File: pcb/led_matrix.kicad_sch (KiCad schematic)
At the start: 8 parts

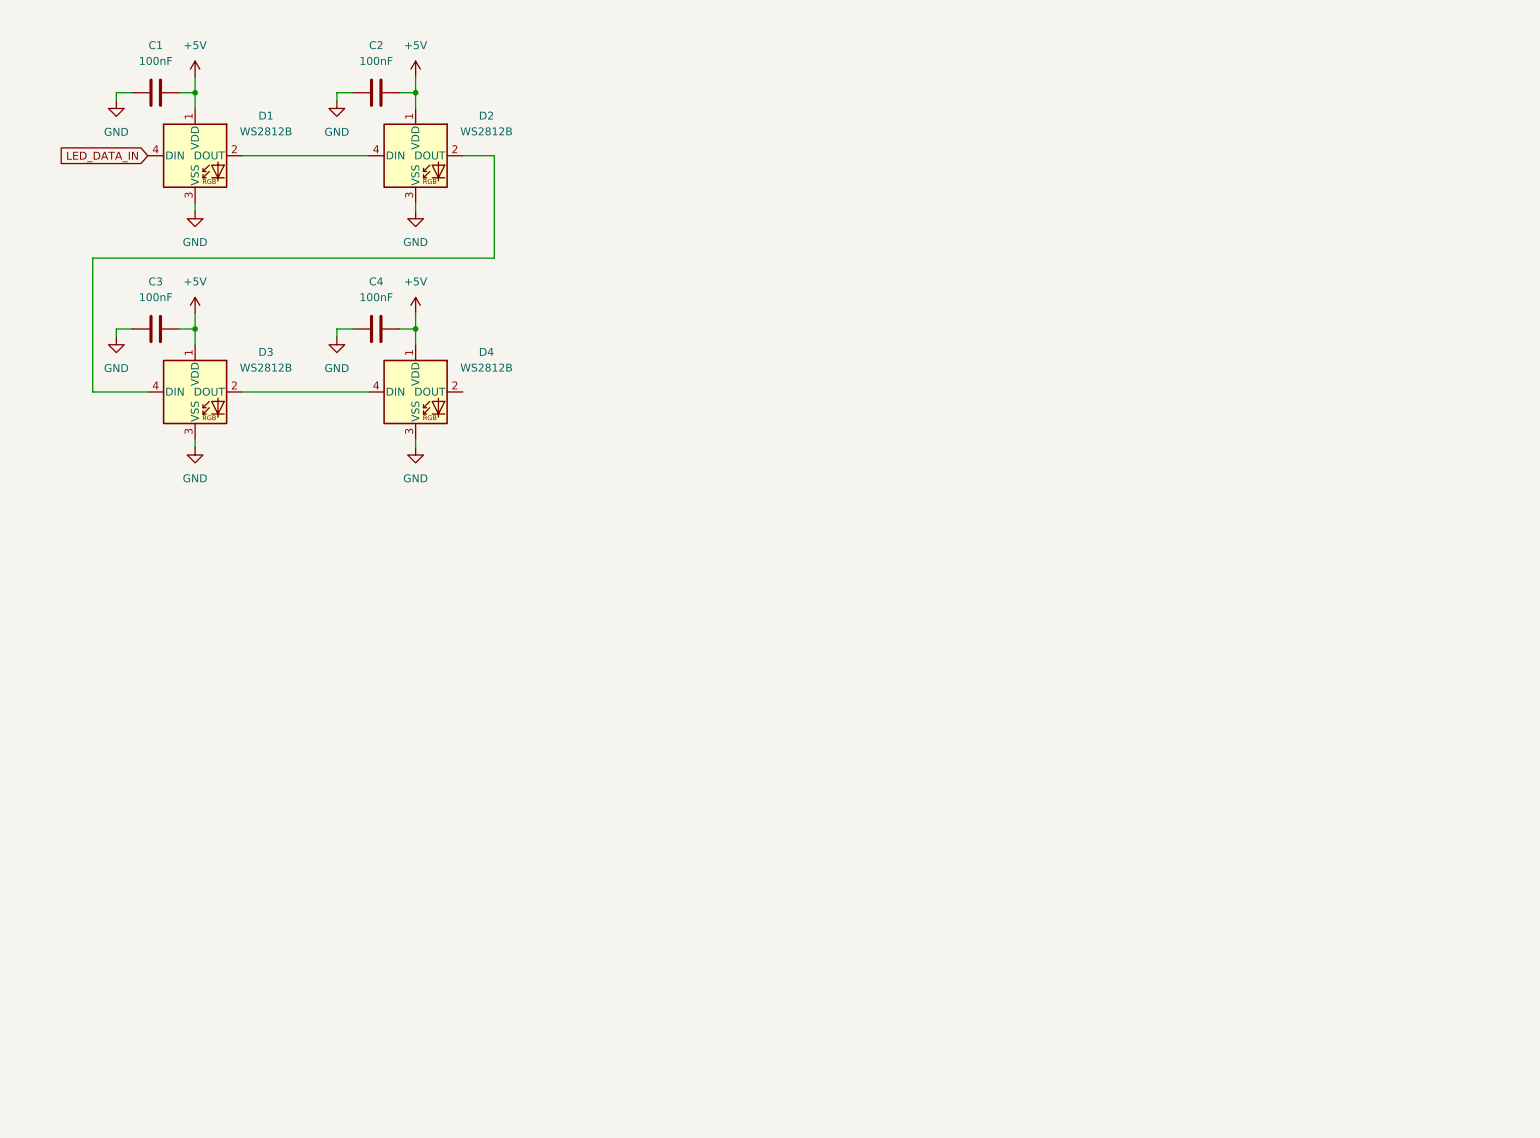
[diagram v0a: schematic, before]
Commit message: connect all components in schematic, only 13 LEDs for now
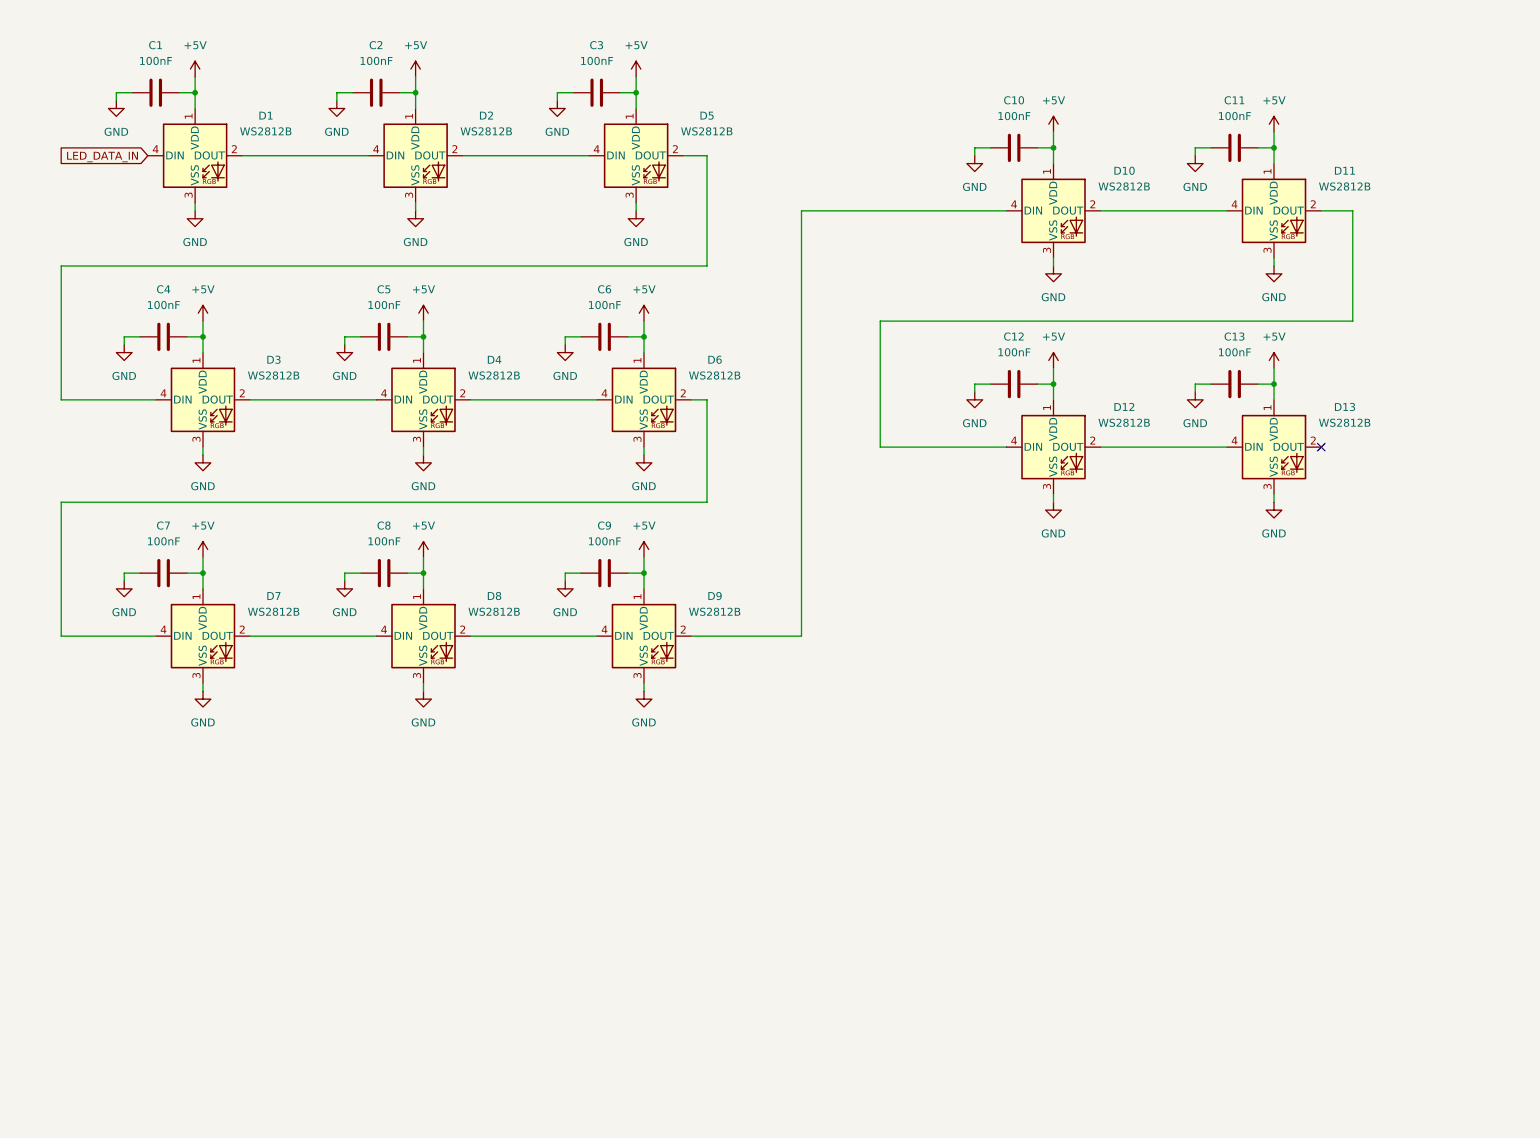
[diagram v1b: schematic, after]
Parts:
- added C10, C11, C12, C13, C5, C6, C7, C8, C9: 100nF, symbol Device:C
- added D10, D11, D12, D13, D5, D6, D7, D8, D9: WS2812B, LED_SMD:LED_WS2812B_PLCC4_5.0x5.0mm_P3.2mm, symbol LED:WS2812B
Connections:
- net +5V: now also C10.2, C11.2, C12.2, C13.2, C5.2, C6.2, C7.2, C8.2, C9.2, D10.1 (VDD), D11.1 (VDD), D12.1 (VDD), D13.1 (VDD), D5.1 (VDD), D6.1 (VDD), D7.1 (VDD), D8.1 (VDD), D9.1 (VDD)
- net GND: now also C10.1, C11.1, C12.1, C13.1, C5.1, C6.1, C7.1, C8.1, C9.1, D10.3 (VSS), D11.3 (VSS), D12.3 (VSS), D13.3 (VSS), D5.3 (VSS), D6.3 (VSS), D7.3 (VSS), D8.3 (VSS), D9.3 (VSS)
- net at D4.2 (DOUT): now also D6.4 (DIN)
- net at D2.2 (DOUT): now also D5.4 (DIN); no longer D3.4 (DIN)
- new net: D3.4 (DIN), D5.2 (DOUT)
- new net: D8.2 (DOUT), D9.4 (DIN)
- new net: D7.2 (DOUT), D8.4 (DIN)
- new net: D10.2 (DOUT), D11.4 (DIN)
- new net: D10.4 (DIN), D9.2 (DOUT)
- new net: D12.2 (DOUT), D13.4 (DIN)
- new net: D6.2 (DOUT), D7.4 (DIN)
- new net: D11.2 (DOUT), D12.4 (DIN)
- no-connect marks 0 -> 1

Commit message: add description to schematic sheets
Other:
- title: (none) -> Project Mora Jai
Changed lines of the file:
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@@
 	(generator_version "9.0")
 	(paper "A4")
+	(title_block
+		(title "Project Mora Jai")
+		(date "2026-02-04")
+		(rev "1")
+		(comment 1 "CERN-OHL-S-2.0")
+	)
 	(junction
 		(at 45.72 66.04)

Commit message: start PCB dimensions
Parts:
- C1, C10, C11, C12, C13, C2, C3, C4, C5, C6, C7, C8, C9: footprint (none) -> Capacitor_SMD:C_0805_2012Metric_Pad1.18x1.45mm_HandSolder
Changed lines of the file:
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@@
 			)
 		)
-		(property "Footprint" ""
+		(property "Footprint" "Capacitor_SMD:C_0805_2012Metric_Pad1.18x1.45mm_HandSolder"
 			(at 41.91 25.7048 0)
 			(effects
@@
 			)
 		)
-		(property "Footprint" ""
+		(property "Footprint" "Capacitor_SMD:C_0805_2012Metric_Pad1.18x1.45mm_HandSolder"
 			(at 215.9 34.5948 0)
 			(effects
@@
 			)
 		)
-		(property "Footprint" ""
+		(property "Footprint" "Capacitor_SMD:C_0805_2012Metric_Pad1.18x1.45mm_HandSolder"
 			(at 43.18 65.0748 0)
 			(effects
@@
 			)
 		)
-		(property "Footprint" ""
+		(property "Footprint" "Capacitor_SMD:C_0805_2012Metric_Pad1.18x1.45mm_HandSolder"
 			(at 77.47 25.7048 0)
 			(effects
@@
 			)
 		)
-		(property "Footprint" ""
+		(property "Footprint" "Capacitor_SMD:C_0805_2012Metric_Pad1.18x1.45mm_HandSolder"
 			(at 215.9 72.6948 0)
 			(effects
@@
 			)
 		)
-		(property "Footprint" ""
+		(property "Footprint" "Capacitor_SMD:C_0805_2012Metric_Pad1.18x1.45mm_HandSolder"
 			(at 114.3 65.0748 0)
 			(effects
@@
 			)
 		)
-		(property "Footprint" ""
+		(property "Footprint" "Capacitor_SMD:C_0805_2012Metric_Pad1.18x1.45mm_HandSolder"
 			(at 180.34 34.5948 0)
 			(effects
@@
 			)
 		)
-		(property "Footprint" ""
+		(property "Footprint" "Capacitor_SMD:C_0805_2012Metric_Pad1.18x1.45mm_HandSolder"
 			(at 78.74 103.1748 0)
 			(effects
@@
 			)
 		)
-		(property "Footprint" ""
+		(property "Footprint" "Capacitor_SMD:C_0805_2012Metric_Pad1.18x1.45mm_HandSolder"
 			(at 180.34 72.6948 0)
 			(effects
@@
 			)
 		)
-		(property "Footprint" ""
+		(property "Footprint" "Capacitor_SMD:C_0805_2012Metric_Pad1.18x1.45mm_HandSolder"
 			(at 114.3 103.1748 0)
 			(effects
@@
 			)
 		)
-		(property "Footprint" ""
+		(property "Footprint" "Capacitor_SMD:C_0805_2012Metric_Pad1.18x1.45mm_HandSolder"
 			(at 43.18 103.1748 0)
 			(effects
@@
 			)
 		)
-		(property "Footprint" ""
+		(property "Footprint" "Capacitor_SMD:C_0805_2012Metric_Pad1.18x1.45mm_HandSolder"
 			(at 113.03 25.7048 0)
 			(effects
@@
 			)
 		)
-		(property "Footprint" ""
+		(property "Footprint" "Capacitor_SMD:C_0805_2012Metric_Pad1.18x1.45mm_HandSolder"
 			(at 78.74 65.0748 0)
 			(effects

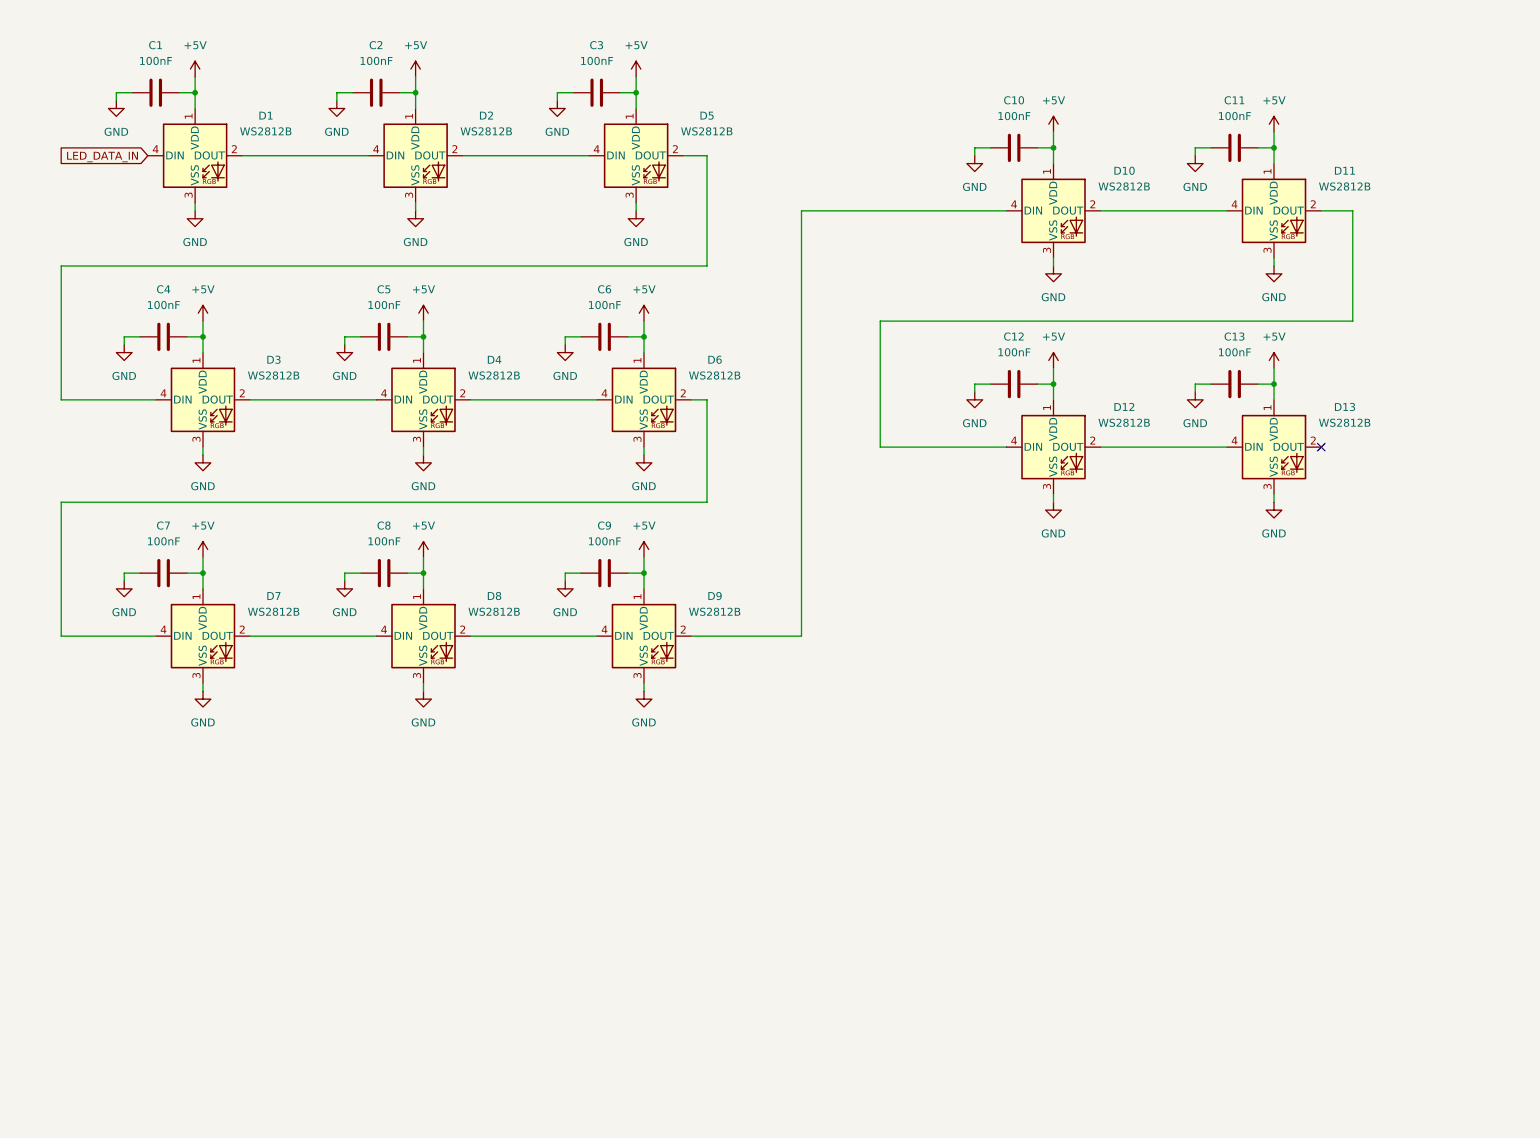
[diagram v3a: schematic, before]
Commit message: add power switch, more LEDs, and custom symbols/footprints to project
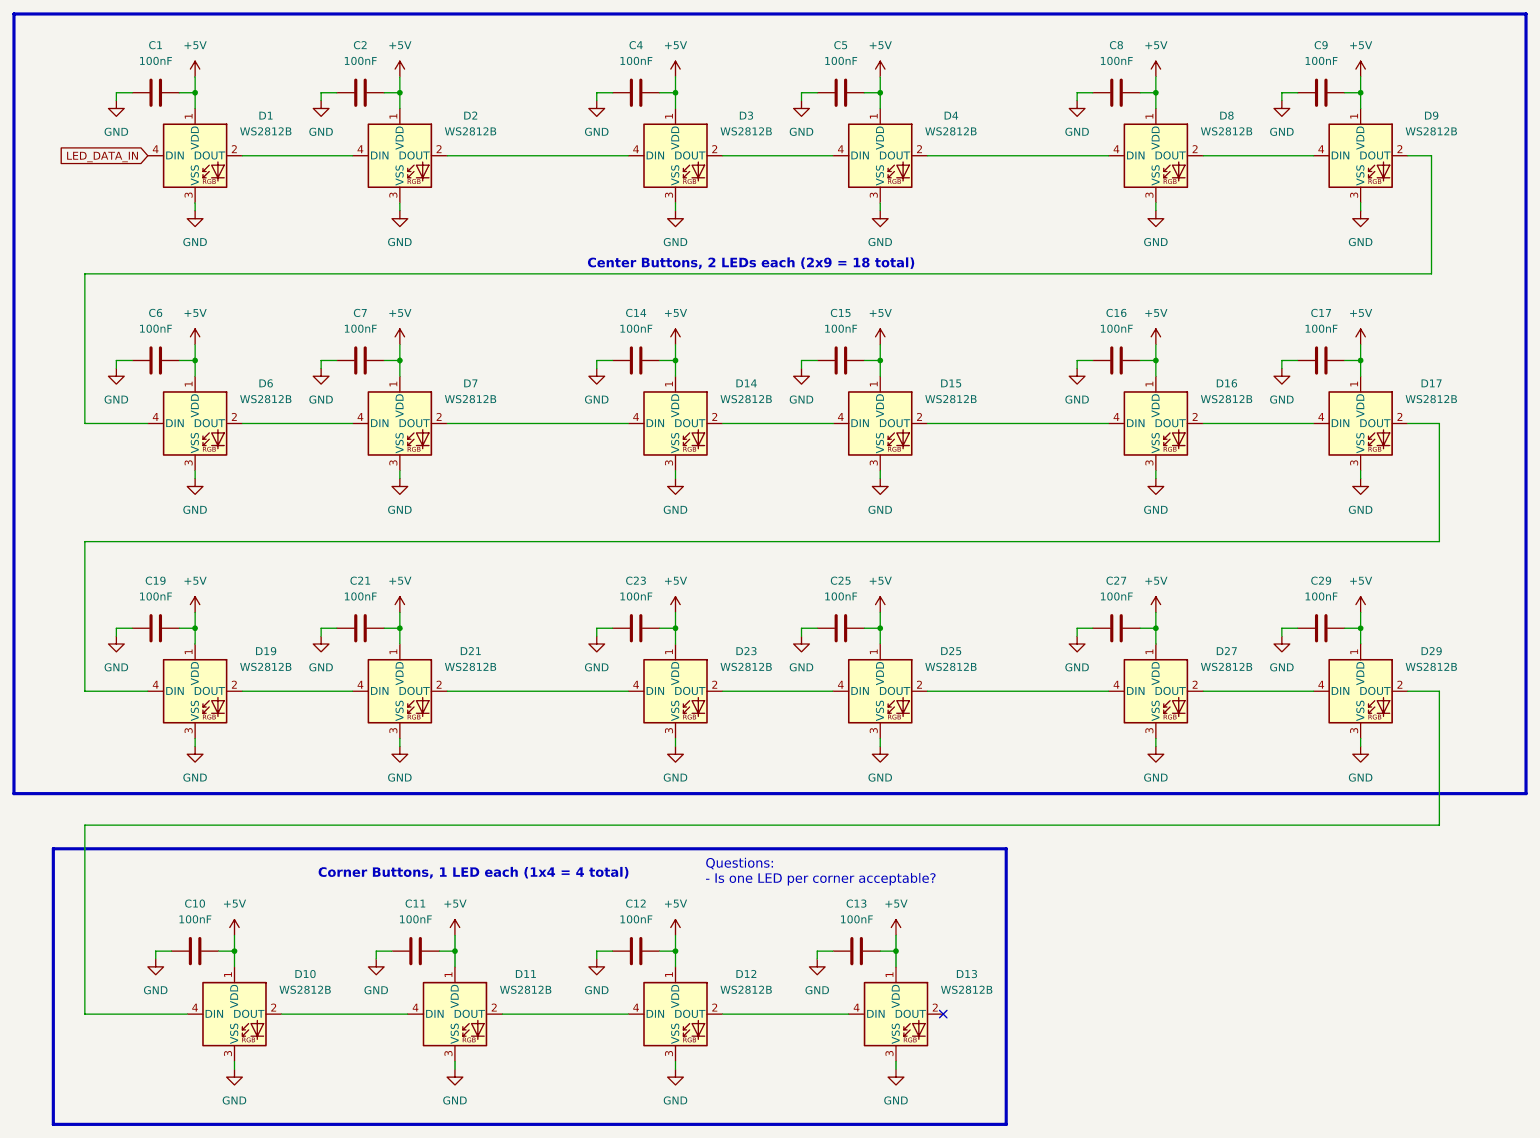
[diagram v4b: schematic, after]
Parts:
- removed C3: 100nF, Capacitor_SMD:C_0805_2012Metric_Pad1.18x1.45mm_HandSolder, symbol Device:C
- removed D5: WS2812B, LED_SMD:LED_WS2812B_PLCC4_5.0x5.0mm_P3.2mm, symbol LED:WS2812B
- added C14, C15, C16, C17, C19, C21, C23, C25, C27, C29: 100nF, Capacitor_SMD:C_0805_2012Metric_Pad1.18x1.45mm_HandSolder, symbol Device:C
- added D14, D15, D16, D17, D19, D21, D23, D25, D27, D29: WS2812B, LED_SMD:LED_WS2812B_PLCC4_5.0x5.0mm_P3.2mm, symbol LED:WS2812B
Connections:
- net +5V: now also C14.2, C15.2, C16.2, C17.2, C19.2, C21.2, C23.2, C25.2, C27.2, C29.2, D14.1 (VDD), D15.1 (VDD), D16.1 (VDD), D17.1 (VDD), D19.1 (VDD), D21.1 (VDD), D23.1 (VDD), D25.1 (VDD), D27.1 (VDD), D29.1 (VDD)
- net GND: now also C14.1, C15.1, C16.1, C17.1, C19.1, C21.1, C23.1, C25.1, C27.1, C29.1, D14.3 (VSS), D15.3 (VSS), D16.3 (VSS), D17.3 (VSS), D19.3 (VSS), D21.3 (VSS), D23.3 (VSS), D25.3 (VSS), D27.3 (VSS), D29.3 (VSS)
- net at D2.2 (DOUT): now also D3.4 (DIN)
- net at D8.4 (DIN): now also D4.2 (DOUT); no longer D7.2 (DOUT)
- net at D10.4 (DIN): now also D29.2 (DOUT); no longer D9.2 (DOUT)
- net at D6.4 (DIN): now also D9.2 (DOUT); no longer D4.2 (DOUT)
- new net: D21.2 (DOUT), D23.4 (DIN)
- new net: D19.2 (DOUT), D21.4 (DIN)
- new net: D16.2 (DOUT), D17.4 (DIN)
- new net: D15.2 (DOUT), D16.4 (DIN)
- new net: D27.2 (DOUT), D29.4 (DIN)
- new net: D25.2 (DOUT), D27.4 (DIN)
- new net: D23.2 (DOUT), D25.4 (DIN)
- new net: D14.2 (DOUT), D15.4 (DIN)
- new net: D14.4 (DIN), D7.2 (DOUT)
- new net: D17.2 (DOUT), D19.4 (DIN)
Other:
- note added: "Center Buttons, 2 LEDs each (2x9 = 18 total)"
- note added: "Corner Buttons, 1 LED each (1x4 = 4 total)"
- note added: "Questions: - Is one LED per corner acceptable?"
- moved on the sheet: C10, C11, C12, C13, C2, D10, D11, D12, D13, D2
